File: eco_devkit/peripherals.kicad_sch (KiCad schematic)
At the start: 39 parts, among them J4 ADC_SEL1, J5 BluetoothHeader, Q1 MOSFET, Q2 MMBT3904, Q5 MOSFET, Q6 OP598A, SW3 PTS636, SW4 PTS636, SW5 PTS636, SW6 PTS636

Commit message: Notate schematic.
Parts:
- renumbered D8 to D7, Q5 to Q3, Q6 to Q4, R51 to R23, R23 to R24, R50 to R25, R24 to R26, R52 to R27, R25 to R28, R26 to R29
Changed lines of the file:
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@@
 		(dnp no)
 		(fields_autoplaced yes)
-		(property "Reference" "#PWR095"
+		(property "Reference" "#PWR038"
 			(at 217.17 143.51 0)
 			(effects
@@
 			(project "eco_devkit"
 				(path "/308cd3d6-c3d9-49fe-9127-06fda61df52b/146c382c-2a6c-4a12-90a2-a26f2a1dd60b"
-					(reference "#PWR095")
+					(reference "#PWR038")
 					(unit 1)
 				)
@@
 		(dnp no)
 		(fields_autoplaced yes)
-		(property "Reference" "R26"
+		(property "Reference" "R29"
 			(at 260.35 45.7199 0)
 			(effects
@@
 			(project "eco_devkit"
 				(path "/308cd3d6-c3d9-49fe-9127-06fda61df52b/146c382c-2a6c-4a12-90a2-a26f2a1dd60b"
-					(reference "R26")
+					(reference "R29")
 					(unit 1)
 				)
@@
 		(dnp no)
 		(fields_autoplaced yes)
-		(property "Reference" "#PWR038"
+		(property "Reference" "#PWR040"
 			(at 227.33 72.39 0)
 			(effects
@@
 			(project ""
 				(path "/308cd3d6-c3d9-49fe-9127-06fda61df52b/146c382c-2a6c-4a12-90a2-a26f2a1dd60b"
-					(reference "#PWR038")
+					(reference "#PWR040")
 					(unit 1)
 				)
@@
 		(dnp no)
 		(fields_autoplaced yes)
-		(property "Reference" "D8"
+		(property "Reference" "D7"
 			(at 219.71 114.1729 90)
 			(effects
@@
 			(project ""
 				(path "/308cd3d6-c3d9-49fe-9127-06fda61df52b/146c382c-2a6c-4a12-90a2-a26f2a1dd60b"
-					(reference "D8")
+					(reference "D7")
 					(unit 1)
 				)
@@
 		(dnp no)
 		(fields_autoplaced yes)
-		(property "Reference" "#PWR094"
+		(property "Reference" "#PWR037"
 			(at 217.17 106.68 0)
 			(effects
@@
 			(project "eco_devkit"
 				(path "/308cd3d6-c3d9-49fe-9127-06fda61df52b/146c382c-2a6c-4a12-90a2-a26f2a1dd60b"
-					(reference "#PWR094")
+					(reference "#PWR037")
 					(unit 1)
 				)
@@
 		(dnp no)
 		(fields_autoplaced yes)
-		(property "Reference" "#PWR097"
+		(property "Reference" "#PWR041"
 			(at 247.65 106.68 0)
 			(effects
@@
 			(project "eco_devkit"
 				(path "/308cd3d6-c3d9-49fe-9127-06fda61df52b/146c382c-2a6c-4a12-90a2-a26f2a1dd60b"
-					(reference "#PWR097")
+					(reference "#PWR041")
 					(unit 1)
 				)
@@
 		(dnp no)
 		(fields_autoplaced yes)
-		(property "Reference" "R23"
+		(property "Reference" "R24"
 			(at 219.71 45.7199 0)
 			(effects
@@
 			(project "eco_devkit"
 				(path "/308cd3d6-c3d9-49fe-9127-06fda61df52b/146c382c-2a6c-4a12-90a2-a26f2a1dd60b"
-					(reference "R23")
+					(reference "R24")
 					(unit 1)
 				)
@@
 		(on_board yes)
 		(dnp no)
-		(property "Reference" "R51"
+		(property "Reference" "R23"
 			(at 201.676 120.396 0)
 			(effects
@@
 			(project "eco_devkit"
 				(path "/308cd3d6-c3d9-49fe-9127-06fda61df52b/146c382c-2a6c-4a12-90a2-a26f2a1dd60b"
-					(reference "R51")
+					(reference "R23")
 					(unit 1)
 				)
@@
 		(on_board yes)
 		(dnp no)
-		(property "Reference" "#PWR039"
+		(property "Reference" "#PWR043"
 			(at 248.92 45.72 0)
 			(effects
@@
 			(project ""
 				(path "/308cd3d6-c3d9-49fe-9127-06fda61df52b/146c382c-2a6c-4a12-90a2-a26f2a1dd60b"
-					(reference "#PWR039")
+					(reference "#PWR043")
 					(unit 1)
 				)
@@
 		(on_board yes)
 		(dnp no)
-		(property "Reference" "R52"
+		(property "Reference" "R27"
 			(at 250.19 128.2699 0)
 			(effects
@@
 			(project "eco_devkit"
 				(path "/308cd3d6-c3d9-49fe-9127-06fda61df52b/146c382c-2a6c-4a12-90a2-a26f2a1dd60b"
-					(reference "R52")
+					(reference "R27")
 					(unit 1)
 				)
@@
 		(dnp no)
 		(fields_autoplaced yes)
-		(property "Reference" "Q5"
+		(property "Reference" "Q3"
 			(at 220.98 125.7299 0)
 			(effects
@@
 			(project "eco_devkit"
 				(path "/308cd3d6-c3d9-49fe-9127-06fda61df52b/146c382c-2a6c-4a12-90a2-a26f2a1dd60b"
-					(reference "Q5")
+					(reference "Q3")
 					(unit 1)
 				)
@@
 		(on_board yes)
 		(dnp no)
-		(property "Reference" "R50"
+		(property "Reference" "R25"
 			(at 214.122 106.68 0)
 			(effects
@@
 			(project "eco_devkit"
 				(path "/308cd3d6-c3d9-49fe-9127-06fda61df52b/146c382c-2a6c-4a12-90a2-a26f2a1dd60b"
-					(reference "R50")
+					(reference "R25")
 					(unit 1)
 				)
@@
 		(dnp no)
 		(fields_autoplaced yes)
-		(property "Reference" "Q6"
+		(property "Reference" "Q4"
 			(at 250.19 117.3606 0)
 			(effects
@@
 			(project ""
 				(path "/308cd3d6-c3d9-49fe-9127-06fda61df52b/146c382c-2a6c-4a12-90a2-a26f2a1dd60b"
-					(reference "Q6")
+					(reference "Q4")
 					(unit 1)
 				)
@@
 		(on_board yes)
 		(dnp no)
-		(property "Reference" "#PWR037"
+		(property "Reference" "#PWR039"
 			(at 220.98 44.45 0)
 			(effects
@@
 			(project "eco_devkit"
 				(path "/308cd3d6-c3d9-49fe-9127-06fda61df52b/146c382c-2a6c-4a12-90a2-a26f2a1dd60b"
-					(reference "#PWR037")
+					(reference "#PWR039")
 					(unit 1)
 				)
@@
 		(dnp no)
 		(fields_autoplaced yes)
-		(property "Reference" "#PWR096"
+		(property "Reference" "#PWR042"
 			(at 247.65 142.24 0)
 			(effects
@@
 			(project "eco_devkit"
 				(path "/308cd3d6-c3d9-49fe-9127-06fda61df52b/146c382c-2a6c-4a12-90a2-a26f2a1dd60b"
-					(reference "#PWR096")
+					(reference "#PWR042")
 					(unit 1)
 				)
@@
 		(on_board yes)
 		(dnp no)
-		(property "Reference" "R25"
+		(property "Reference" "R28"
 			(at 251.46 45.7199 0)
 			(effects
@@
 			(project "eco_devkit"
 				(path "/308cd3d6-c3d9-49fe-9127-06fda61df52b/146c382c-2a6c-4a12-90a2-a26f2a1dd60b"
-					(reference "R25")
+					(reference "R28")
 					(unit 1)
 				)
@@
 		(dnp no)
 		(fields_autoplaced yes)
-		(property "Reference" "R24"
+		(property "Reference" "R26"
 			(at 228.6 45.7199 0)
 			(effects
@@
 			(project "eco_devkit"
 				(path "/308cd3d6-c3d9-49fe-9127-06fda61df52b/146c382c-2a6c-4a12-90a2-a26f2a1dd60b"
-					(reference "R24")
+					(reference "R26")
 					(unit 1)
 				)

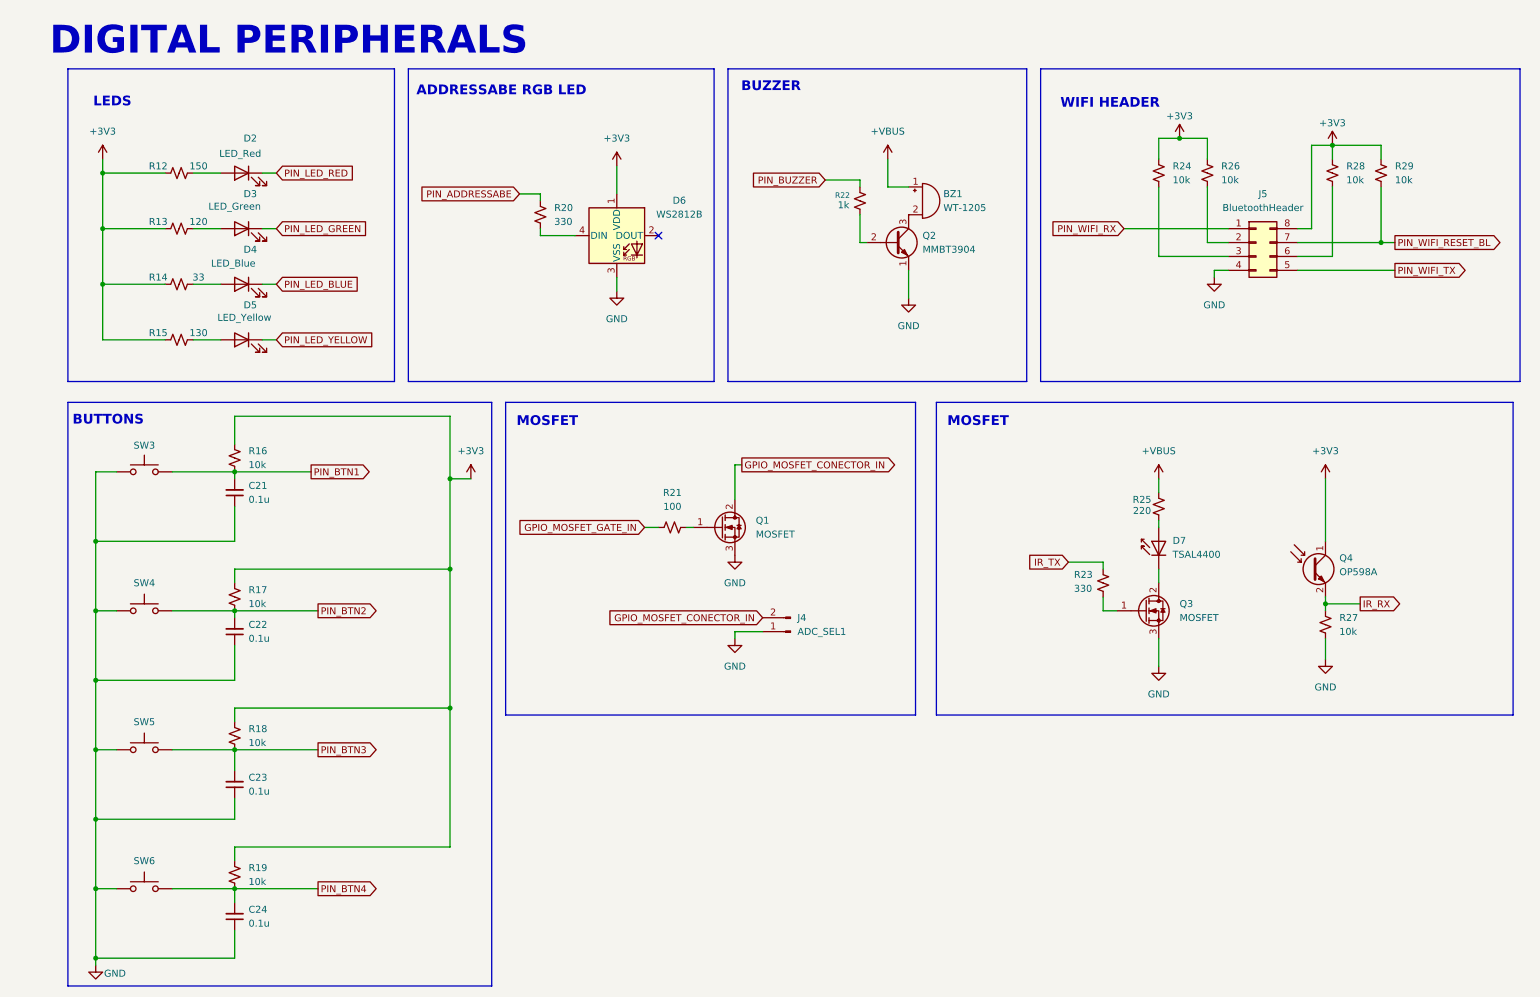
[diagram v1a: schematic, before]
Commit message: Corrige folha dos perifericos
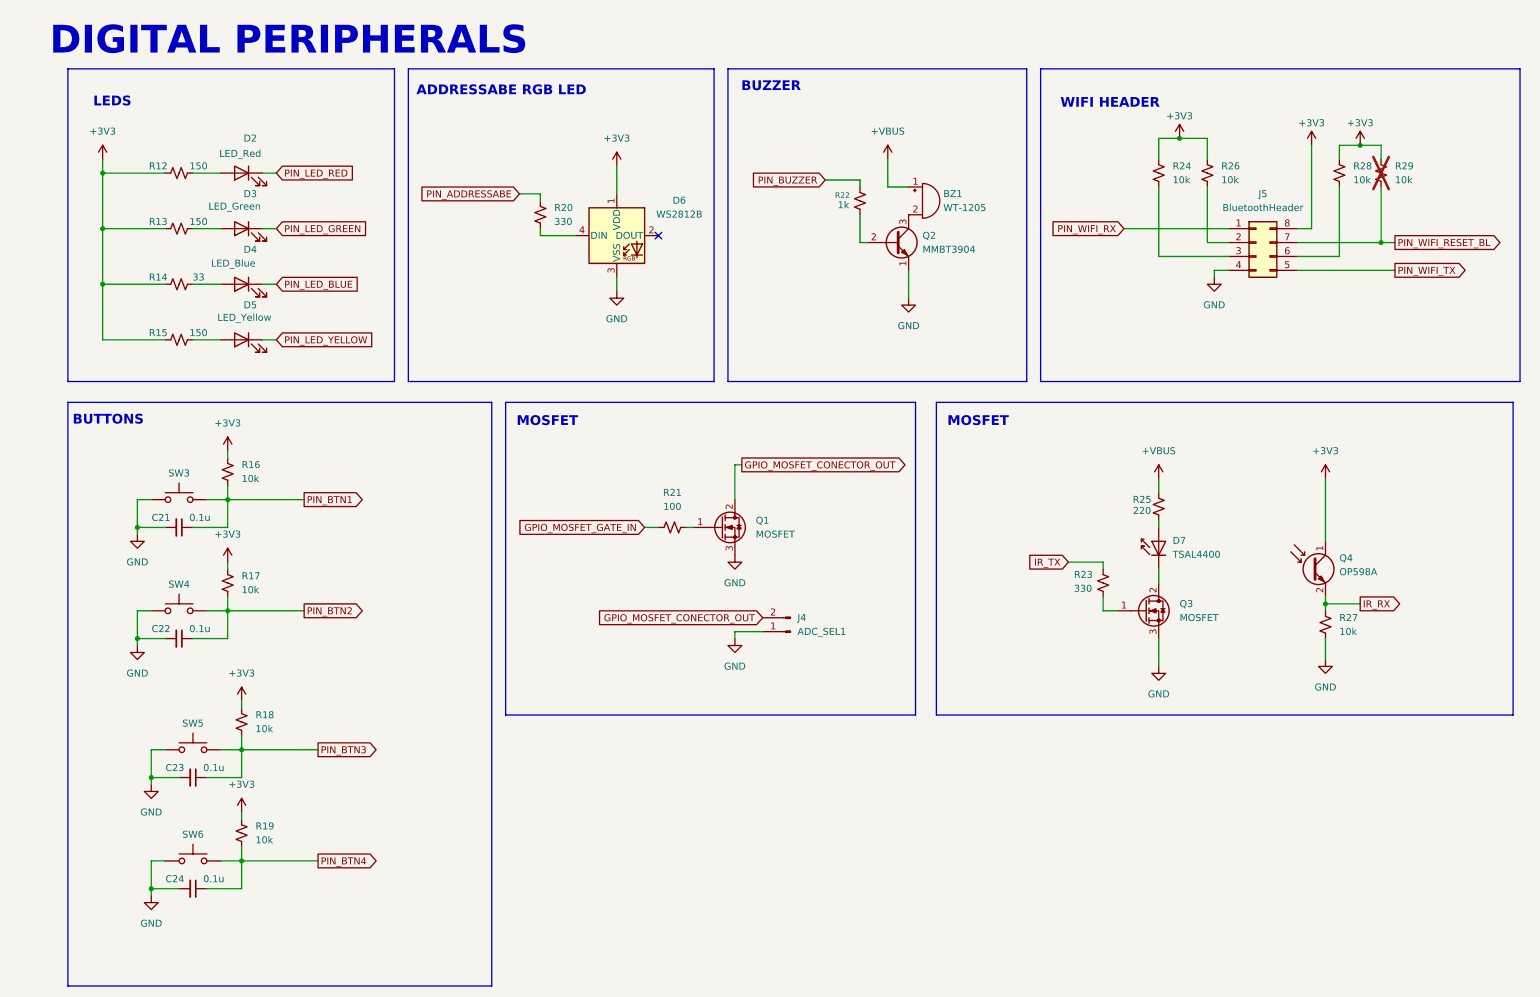
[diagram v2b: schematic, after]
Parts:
- R13: value 120 -> 150
- R15: value 130 -> 150
- R29: now not fitted
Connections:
- net GND: now also C21.2, C22.2, C23.2, C24.2; no longer C21.1, C22.1, C23.1, C24.1
- net PIN_BTN1: now also C21.1; no longer C21.2
- net PIN_BTN2: now also C22.1; no longer C22.2
- net PIN_BTN3: now also C23.1; no longer C23.2
- net PIN_BTN4: now also C24.1; no longer C24.2
- net GPIO_MOSFET_CONECTOR_IN renamed GPIO_MOSFET_CONECTOR_OUT
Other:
- moved on the sheet: C21, R16, R28, SW3
